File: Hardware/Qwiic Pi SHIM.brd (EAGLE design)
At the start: 10.2 x 14 mm, 14 parts, among them J1 Qwiic Right Angle, U2 3.3V/600mA

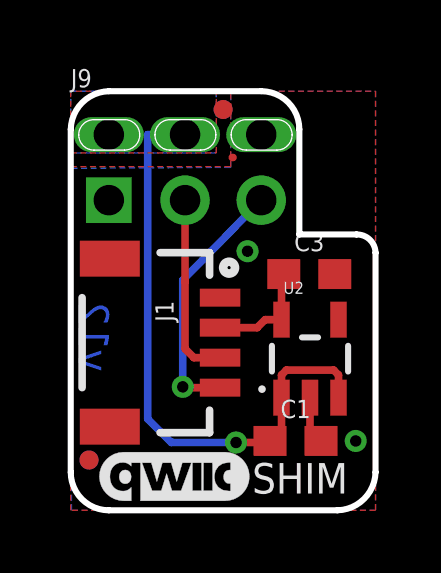
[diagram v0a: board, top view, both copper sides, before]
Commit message: Reverting to tighter spacing (aka v14 or "4MILS")
-updated single brd files, panel files (and production gerbers)
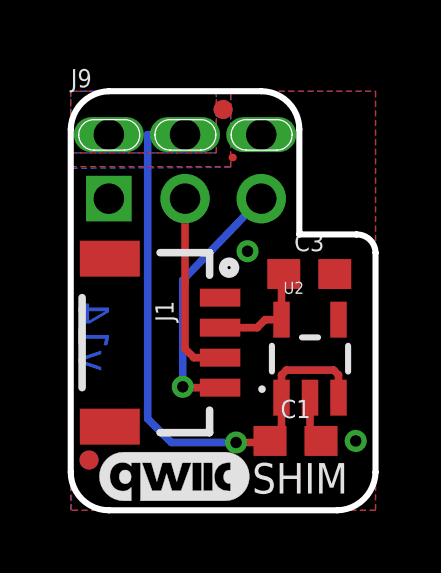
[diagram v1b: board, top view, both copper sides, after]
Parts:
- J9: device Qwiic Pi SHIM:SPARKFUN-CONNECTORS_2X3-NS_PISHIM_LOCKING_SLOTS-2MILS -> Qwiic Pi SHIM:SPARKFUN-CONNECTORS_2X3-NS_PISHIM_LOCKING_SLOTS-4MILS
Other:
- board text added: "v14"
- board text removed: "v12"
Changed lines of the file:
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@@
 <plain>
 <text x="20.32" y="-13.97" size="1.778" layer="51" font="vector">Pete Lewis</text>
-<text x="1.27" y="6.9596" size="1.016" layer="16" font="vector" ratio="20" rot="MR270">v12</text>
+<text x="1.27" y="6.9596" size="1.016" layer="16" font="vector" ratio="20" rot="MR270">v14</text>
 <text x="6.0452" y="0.5588" size="1.016" layer="21" font="vector" ratio="15">SHIM</text>
 <dimension x1="0" y1="0" x2="0" y2="13.97" x3="-6.35" y3="6.985" textsize="1.27" layer="47" unit="inch" visible="yes"/>
@@
 <element name="FD3" library="SparkFun-Aesthetics" package="FIDUCIAL-MICRO" value="FIDUCIALUFIDUCIAL" x="0.6096" y="1.6764" smashed="yes" rot="MR0"/>
 <element name="FD4" library="SparkFun-Aesthetics" package="FIDUCIAL-MICRO" value="FIDUCIALUFIDUCIAL" x="5.08" y="13.3604" smashed="yes" rot="MR0"/>
-<element name="J9" library="Qwiic Pi SHIM" package="SPARKFUN-CONNECTORS_2X3-NS_PISHIM_LOCKING_SLOTS-2MILS" value="" x="3.81" y="11.43" smashed="yes">
+<element name="J9" library="Qwiic Pi SHIM" package="SPARKFUN-CONNECTORS_2X3-NS_PISHIM_LOCKING_SLOTS-4MILS" value="" x="3.81" y="11.43" smashed="yes">
 <attribute name="NAME" x="0" y="14.097" size="0.6096" layer="25" font="vector" ratio="20"/>
 <attribute name="VALUE" x="0" y="7.493" size="0.6096" layer="27" font="vector" ratio="20"/>
@@
 <contactref element="J9" pad="3"/>
 <wire x1="3.81" y1="5.3848" x2="3.81" y2="7.62" width="0.254" layer="1"/>
-<wire x1="3.81" y1="7.62" x2="3.81" y2="10.3378" width="0.254" layer="1"/>
+<wire x1="3.81" y1="7.62" x2="3.81" y2="10.3886" width="0.254" layer="1"/>
 <wire x1="4.9784" y1="5.088" x2="4.1068" y2="5.088" width="0.254" layer="1"/>
 <wire x1="4.1068" y1="5.088" x2="3.81" y2="5.3848" width="0.254" layer="1"/>
@@
 <wire x1="4.9784" y1="4.088" x2="3.7606" y2="4.088" width="0.254" layer="1"/>
 <wire x1="3.7606" y1="4.088" x2="3.7338" y2="4.1148" width="0.254" layer="1"/>
-<wire x1="3.7338" y1="7.6708" x2="6.35" y2="10.3378" width="0.254" layer="16"/>
+<wire x1="3.7338" y1="7.6708" x2="6.35" y2="10.3886" width="0.254" layer="16"/>
 <wire x1="3.7338" y1="4.1148" x2="3.7338" y2="7.6708" width="0.254" layer="16"/>
 </signal>
